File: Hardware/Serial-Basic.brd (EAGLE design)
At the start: 22.9 x 16.5 mm, 25 parts, among them J1 microB, U1 AP2112-3.3V, U2 CH340G, Y2 12MHz

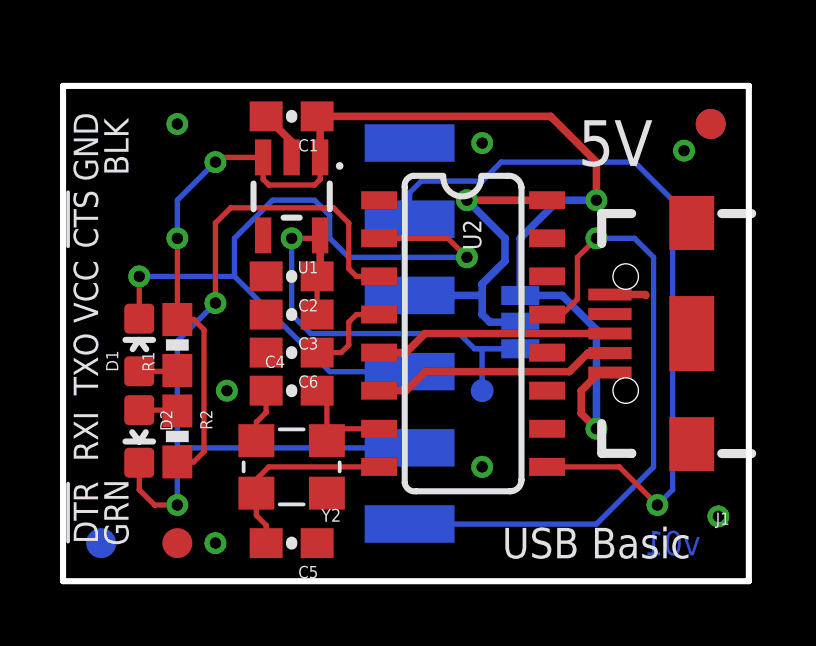
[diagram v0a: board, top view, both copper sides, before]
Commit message: Many hardware changes from review.
Moved 0.1uF closer to IC, changed to VCC net. Added via anchors to
microB. Silk bumps. PCB width increase.
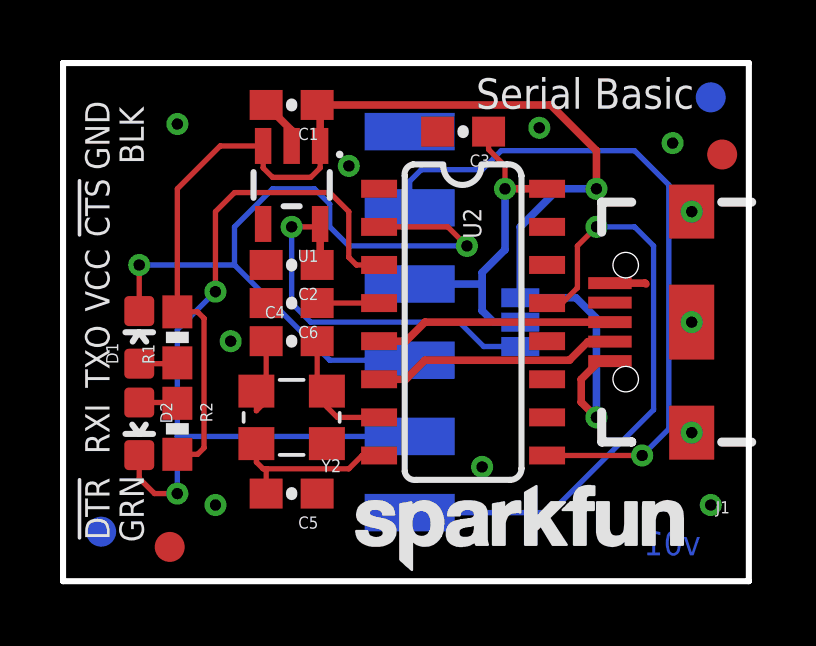
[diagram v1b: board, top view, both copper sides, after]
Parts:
- removed SJ1: (no value), SparkFun:SJ_3
- removed TP1: 3.3V TP, SparkFun-Passives:PAD.03X.03
- added JP1: (no value), SparkFun-Passives:PAD-JUMPER-3-2OF3_NC_BY_PASTE_YES_SILK_FULL_BOX
- moved LOGO3 20.0 mm to (9.27, -0.13), flipped to the top, turned to 0 degrees
- moved C3 8.36 mm to (13.3, 15.0)
- moved LOGO1 4.65 mm to (21.0, 10.5), turned to 270 degrees
- moved LOGO2 2.44 mm to (22.5, 7.87)
- moved C6 1.65 mm to (7.62, 9.27)
- moved Y2 1.65 mm to (7.62, 5.46)
- moved C4 1.65 mm to (7.62, 8.00)
- moved C5 1.65 mm to (7.62, 2.92)
- moved JP4 1.09 mm to (22.0, 14.2)
- moved JP6 0.89 mm to (21.6, 16.1)
- moved C1 0.38 mm to (7.62, 15.9)
- moved C2 0.38 mm to (7.62, 10.5)
- moved U1 0.38 mm to (7.62, 13.2)
- moved JP5 0.38 mm to (1.27, 1.65)
- moved J1 0.38 mm to (21.0, 8.64)
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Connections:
- net 3.3V: now also JP1.3; no longer C3.1, SJ1.3, TP1.P$1
- net 5V: now also JP1.1; no longer SJ1.1
- net GND: no longer J1.SHIELD1, J1.SHIELD2, J1.SHIELD3
- net VCC: now also C3.1, JP1.2; no longer SJ1.2
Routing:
- net 3.3V: track 15.7 -> 13.2 mm
- net !CTS: track 25.2 -> 23.0 mm
- net GND: track 4.73 -> 6.04 mm, vias 7 -> 11
- net V3: track 3.04 -> 2.06 mm
- net !DTR: track 21.6 -> 20.7 mm
- net N$3: track 6.52 -> 5.82 mm
- net VCC: track 11.1 -> 11.8 mm
- net 5V: track 43.7 -> 44.3 mm, vias 4 -> 2
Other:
- board size 22.9 x 16.5 mm -> 22.9 x 17.3 mm
- board text added: "All dimensions in inches"
- board text added: "Serial Basic"
- board text removed: "USB Basic"

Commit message: Fixing issues #1, #2, #3, #4
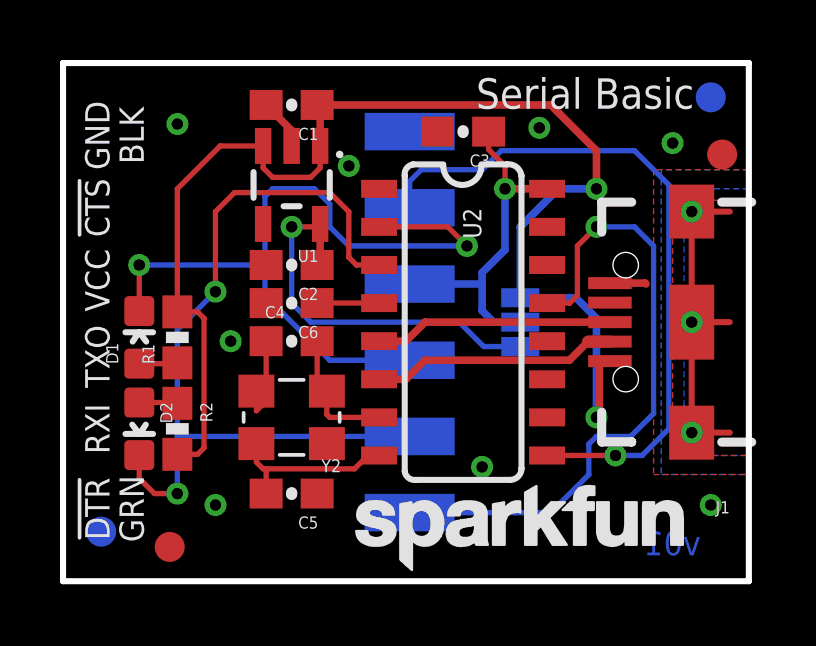
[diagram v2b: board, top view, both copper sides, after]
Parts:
- renumbered J3 to J2
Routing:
- net SHLD: track 0.00 -> 11.2 mm, vias 0 -> 3
- net !DTR: track 20.7 -> 21.5 mm
- net GND: vias 11 -> 8
- added copper zone on layer 1, net SHLD
- added copper zone on layer 16, net SHLD

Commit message: Changing resistor on Greeg LED to 330
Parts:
- R3: value 1K -> 330
- moved JP1 2.54 mm to (17.8, 8.64)
- moved JP5 0.38 mm to (1.27, 1.27)
- renumbered R1 to R3
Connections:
- net 5V: no longer R2.2, R3.2
- net VCC: now also R2.2, R3.2
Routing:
- net VCC: track 11.8 -> 49.9 mm, vias 1 -> 2
- net 5V: track 43.9 -> 32.5 mm
- net !CTS: track 23.0 -> 30.5 mm
- net 3.3V: track 13.2 -> 15.7 mm
- net TXO: track 26.0 -> 24.5 mm
- net GND: vias 8 -> 9
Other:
- board text added: "v10"
- board text removed: "v01"
